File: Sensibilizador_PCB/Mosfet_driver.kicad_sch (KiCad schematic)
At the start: 11 parts, among them U1 LM5104M

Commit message: Rectificador primera versión
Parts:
- renumbered C2 to C?, C1 to C?, C3 to C?, D2 to D?, D1 to D?, R4 to R?, R2 to R?, R3 to R?, R1 to R?, U1 to U?
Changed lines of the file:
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@@
     (effects (font (size 1.27 1.27)) (justify left))
   )
-  (symbol (lib_id "Device:C_Polarized") (at 58.42 67.31 0) (unit 1)
+  (symbol (lib_id "Device:C_Polarized") (at 58.42 67.31 0)
     (in_bom yes) (on_board yes)
-    (property "Reference" "C2" (id 0) (at 64.77 68.58 90)
+    (property "Reference" "C?" (id 0) (at 64.77 68.58 90)
       (effects (font (size 1.27 1.27)) (justify left))
     )
@@
     (pin "2")
   )
-  (symbol (lib_id "Device:R") (at 105.41 80.01 0) (unit 1)
+  (symbol (lib_id "Device:R") (at 105.41 80.01 0)
     (in_bom yes) (on_board yes) (fields_autoplaced)
-    (property "Reference" "R4" (id 0) (at 107.95 78.7399 0)
+    (property "Reference" "R?" (id 0) (at 107.95 78.7399 0)
       (effects (font (size 1.27 1.27)) (justify left))
     )
@@
     (pin "2")
   )
-  (symbol (lib_id "Device:C_Polarized") (at 48.26 67.31 0) (unit 1)
+  (symbol (lib_id "Device:C_Polarized") (at 48.26 67.31 0)
     (in_bom yes) (on_board yes)
-    (property "Reference" "C1" (id 0) (at 52.07 68.58 90)
+    (property "Reference" "C?" (id 0) (at 52.07 68.58 90)
       (effects (font (size 1.27 1.27)) (justify left))
     )
@@
     (pin "2")
   )
-  (symbol (lib_id "Device:R") (at 109.22 63.5 90) (unit 1)
+  (symbol (lib_id "Device:R") (at 109.22 63.5 90)
     (in_bom yes) (on_board yes)
-    (property "Reference" "R2" (id 0) (at 109.22 60.96 90))
+    (property "Reference" "R?" (id 0) (at 109.22 60.96 90))
     (property "Value" " 2.74 1{slash}4W" (id 1) (at 109.22 66.04 90))
     (property "Footprint" "Resistor_SMD:R_1206_3216Metric_Pad1.30x1.75mm_HandSolder" (id 2) (at 109.22 65.278 90)
@@
     (pin "2")
   )
-  (symbol (lib_id "Device:D") (at 118.11 63.5 0) (unit 1)
+  (symbol (lib_id "Device:D") (at 118.11 63.5 0)
     (in_bom yes) (on_board yes)
-    (property "Reference" "D2" (id 0) (at 119.38 60.96 0))
+    (property "Reference" "D?" (id 0) (at 119.38 60.96 0))
     (property "Value" "SS34FA" (id 1) (at 119.38 66.04 0))
     (property "Footprint" "Diode_SMD:D_SOD-123" (id 2) (at 118.11 63.5 0)
@@
     (pin "2")
   )
-  (symbol (lib_id "Device:R") (at 115.57 68.58 90) (unit 1)
+  (symbol (lib_id "Device:R") (at 115.57 68.58 90)
     (in_bom yes) (on_board yes)
-    (property "Reference" "R3" (id 0) (at 115.57 71.12 90))
+    (property "Reference" "R?" (id 0) (at 115.57 71.12 90))
     (property "Value" " 2.74 1{slash}4W" (id 1) (at 115.57 73.66 90))
     (property "Footprint" "Resistor_SMD:R_1206_3216Metric_Pad1.30x1.75mm_HandSolder" (id 2) (at 115.57 70.358 90)
@@
     (pin "2")
   )
-  (symbol (lib_id "Device:C_Polarized") (at 88.9 39.37 90) (unit 1)
+  (symbol (lib_id "Device:C_Polarized") (at 88.9 39.37 90)
     (in_bom yes) (on_board yes)
-    (property "Reference" "C3" (id 0) (at 90.17 33.02 90)
+    (property "Reference" "C?" (id 0) (at 90.17 33.02 90)
       (effects (font (size 1.27 1.27)) (justify left))
     )
@@
     (pin "2")
   )
-  (symbol (lib_id "Device:R") (at 109.22 45.72 90) (unit 1)
+  (symbol (lib_id "Device:R") (at 109.22 45.72 90)
     (in_bom yes) (on_board yes)
-    (property "Reference" "R1" (id 0) (at 109.22 48.26 90))
+    (property "Reference" "R?" (id 0) (at 109.22 48.26 90))
     (property "Value" " 2.74 1{slash}4W" (id 1) (at 109.22 43.18 90))
     (property "Footprint" "Resistor_SMD:R_1206_3216Metric_Pad1.30x1.75mm_HandSolder" (id 2) (at 109.22 47.498 90)
@@
     (pin "2")
   )
-  (symbol (lib_id "Device:D") (at 118.11 45.72 0) (unit 1)
+  (symbol (lib_id "Device:D") (at 118.11 45.72 0)
     (in_bom yes) (on_board yes)
-    (property "Reference" "D1" (id 0) (at 120.65 40.64 0))
+    (property "Reference" "D?" (id 0) (at 120.65 40.64 0))
     (property "Value" "SS34FA" (id 1) (at 120.65 43.18 0))
     (property "Footprint" "Diode_SMD:D_SOD-123" (id 2) (at 118.11 45.72 0)
@@
     (pin "2")
   )
-  (symbol (lib_id "Device:R") (at 118.11 52.07 90) (unit 1)
+  (symbol (lib_id "Device:R") (at 118.11 52.07 90)
     (in_bom yes) (on_board yes)
     (property "Reference" "RHon?" (id 0) (at 118.11 54.61 90))
@@
     (pin "2")
   )
-  (symbol (lib_id "LM5104M:LM5104M") (at 82.55 63.5 0) (unit 1)
+  (symbol (lib_id "LM5104M:LM5104M") (at 82.55 63.5 0)
     (in_bom yes) (on_board yes) (fields_autoplaced)
-    (property "Reference" "U1" (id 0) (at 84.4297 43.18 0)
+    (property "Reference" "U?" (id 0) (at 84.4297 43.18 0)
       (effects (font (size 1.27 1.27)) (justify left))
     )

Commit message: Listo pa tirar lineas
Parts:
- R1: renamed from R?; footprint Resistor_SMD:R_1206_3216Metric_Pad1.30x1.75mm_HandSolder -> Resistor_SMD:R_0805_2012Metric_Pad1.20x1.40mm_HandSolder
- U1: renamed from U?; footprint Package_SO:SOIC-8-1EP_3.9x4.9mm_P1.27mm_EP2.29x3mm -> Package_SO:SOIC-8_3.9x4.9mm_P1.27mm
- gave numbers to parts that had none: 9
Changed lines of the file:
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@@
     (effects (font (size 1.27 1.27)) (justify left))
   )
-  (symbol (lib_id "Device:C_Polarized") (at 58.42 67.31 0)
+  (symbol (lib_id "Device:C_Polarized") (at 58.42 67.31 0) (unit 1)
     (in_bom yes) (on_board yes)
-    (property "Reference" "C?" (id 0) (at 64.77 68.58 90)
+    (property "Reference" "C2" (id 0) (at 64.77 68.58 90)
       (effects (font (size 1.27 1.27)) (justify left))
     )
@@
     (pin "2")
   )
-  (symbol (lib_id "Device:R") (at 105.41 80.01 0)
+  (symbol (lib_id "Device:R") (at 105.41 80.01 0) (unit 1)
     (in_bom yes) (on_board yes) (fields_autoplaced)
-    (property "Reference" "R?" (id 0) (at 107.95 78.7399 0)
+    (property "Reference" "R1" (id 0) (at 107.95 78.7399 0)
       (effects (font (size 1.27 1.27)) (justify left))
     )
@@
       (effects (font (size 1.27 1.27)) (justify left))
     )
-    (property "Footprint" "Resistor_SMD:R_1206_3216Metric_Pad1.30x1.75mm_HandSolder" (id 2) (at 103.632 80.01 90)
+    (property "Footprint" "Resistor_SMD:R_0805_2012Metric_Pad1.20x1.40mm_HandSolder" (id 2) (at 103.632 80.01 90)
       (effects (font (size 1.27 1.27)) hide)
     )
@@
     (pin "2")
   )
-  (symbol (lib_id "Device:C_Polarized") (at 48.26 67.31 0)
+  (symbol (lib_id "Device:C_Polarized") (at 48.26 67.31 0) (unit 1)
     (in_bom yes) (on_board yes)
-    (property "Reference" "C?" (id 0) (at 52.07 68.58 90)
+    (property "Reference" "C1" (id 0) (at 52.07 68.58 90)
       (effects (font (size 1.27 1.27)) (justify left))
     )
@@
     (pin "2")
   )
-  (symbol (lib_id "Device:R") (at 109.22 63.5 90)
+  (symbol (lib_id "Device:R") (at 109.22 63.5 90) (unit 1)
     (in_bom yes) (on_board yes)
-    (property "Reference" "R?" (id 0) (at 109.22 60.96 90))
+    (property "Reference" "R3" (id 0) (at 109.22 60.96 90))
     (property "Value" " 2.74 1{slash}4W" (id 1) (at 109.22 66.04 90))
     (property "Footprint" "Resistor_SMD:R_1206_3216Metric_Pad1.30x1.75mm_HandSolder" (id 2) (at 109.22 65.278 90)
@@
     (pin "2")
   )
-  (symbol (lib_id "Device:D") (at 118.11 63.5 0)
+  (symbol (lib_id "Device:D") (at 118.11 63.5 0) (unit 1)
     (in_bom yes) (on_board yes)
-    (property "Reference" "D?" (id 0) (at 119.38 60.96 0))
+    (property "Reference" "D6" (id 0) (at 119.38 60.96 0))
     (property "Value" "SS34FA" (id 1) (at 119.38 66.04 0))
     (property "Footprint" "Diode_SMD:D_SOD-123" (id 2) (at 118.11 63.5 0)
@@
     (pin "2")
   )
-  (symbol (lib_id "Device:R") (at 115.57 68.58 90)
+  (symbol (lib_id "Device:R") (at 115.57 68.58 90) (unit 1)
     (in_bom yes) (on_board yes)
-    (property "Reference" "R?" (id 0) (at 115.57 71.12 90))
+    (property "Reference" "R4" (id 0) (at 115.57 71.12 90))
     (property "Value" " 2.74 1{slash}4W" (id 1) (at 115.57 73.66 90))
     (property "Footprint" "Resistor_SMD:R_1206_3216Metric_Pad1.30x1.75mm_HandSolder" (id 2) (at 115.57 70.358 90)
@@
     (pin "2")
   )
-  (symbol (lib_id "Device:C_Polarized") (at 88.9 39.37 90)
+  (symbol (lib_id "Device:C_Polarized") (at 88.9 39.37 90) (unit 1)
     (in_bom yes) (on_board yes)
-    (property "Reference" "C?" (id 0) (at 90.17 33.02 90)
+    (property "Reference" "C3" (id 0) (at 90.17 33.02 90)
       (effects (font (size 1.27 1.27)) (justify left))
     )
@@
     (pin "2")
   )
-  (symbol (lib_id "Device:R") (at 109.22 45.72 90)
+  (symbol (lib_id "Device:R") (at 109.22 45.72 90) (unit 1)
     (in_bom yes) (on_board yes)
-    (property "Reference" "R?" (id 0) (at 109.22 48.26 90))
+    (property "Reference" "R2" (id 0) (at 109.22 48.26 90))
     (property "Value" " 2.74 1{slash}4W" (id 1) (at 109.22 43.18 90))
     (property "Footprint" "Resistor_SMD:R_1206_3216Metric_Pad1.30x1.75mm_HandSolder" (id 2) (at 109.22 47.498 90)
@@
     (pin "2")
   )
-  (symbol (lib_id "Device:D") (at 118.11 45.72 0)
+  (symbol (lib_id "Device:D") (at 118.11 45.72 0) (unit 1)
     (in_bom yes) (on_board yes)
-    (property "Reference" "D?" (id 0) (at 120.65 40.64 0))
+    (property "Reference" "D5" (id 0) (at 120.65 40.64 0))
     (property "Value" "SS34FA" (id 1) (at 120.65 43.18 0))
     (property "Footprint" "Diode_SMD:D_SOD-123" (id 2) (at 118.11 45.72 0)
@@
     (pin "2")
   )
-  (symbol (lib_id "Device:R") (at 118.11 52.07 90)
+  (symbol (lib_id "Device:R") (at 118.11 52.07 90) (unit 1)
     (in_bom yes) (on_board yes)
-    (property "Reference" "RHon?" (id 0) (at 118.11 54.61 90))
+    (property "Reference" "RHon1" (id 0) (at 118.11 54.61 90))
     (property "Value" " 2.74 1{slash}4W" (id 1) (at 118.11 49.53 90))
     (property "Footprint" "Resistor_SMD:R_1206_3216Metric_Pad1.30x1.75mm_HandSolder" (id 2) (at 118.11 53.848 90)
@@
     (pin "2")
   )
-  (symbol (lib_id "LM5104M:LM5104M") (at 82.55 63.5 0)
+  (symbol (lib_id "LM5104M:LM5104M") (at 82.55 63.5 0) (unit 1)
     (in_bom yes) (on_board yes) (fields_autoplaced)
-    (property "Reference" "U?" (id 0) (at 84.4297 43.18 0)
+    (property "Reference" "U1" (id 0) (at 84.4297 43.18 0)
       (effects (font (size 1.27 1.27)) (justify left))
     )
@@
       (effects (font (size 1.27 1.27)) (justify left))
     )
-    (property "Footprint" "Package_SO:SOIC-8-1EP_3.9x4.9mm_P1.27mm_EP2.29x3mm" (id 2) (at 82.55 63.5 0)
+    (property "Footprint" "Package_SO:SOIC-8_3.9x4.9mm_P1.27mm" (id 2) (at 82.55 63.5 0)
       (effects (font (size 1.27 1.27)) (justify left bottom) hide)
     )

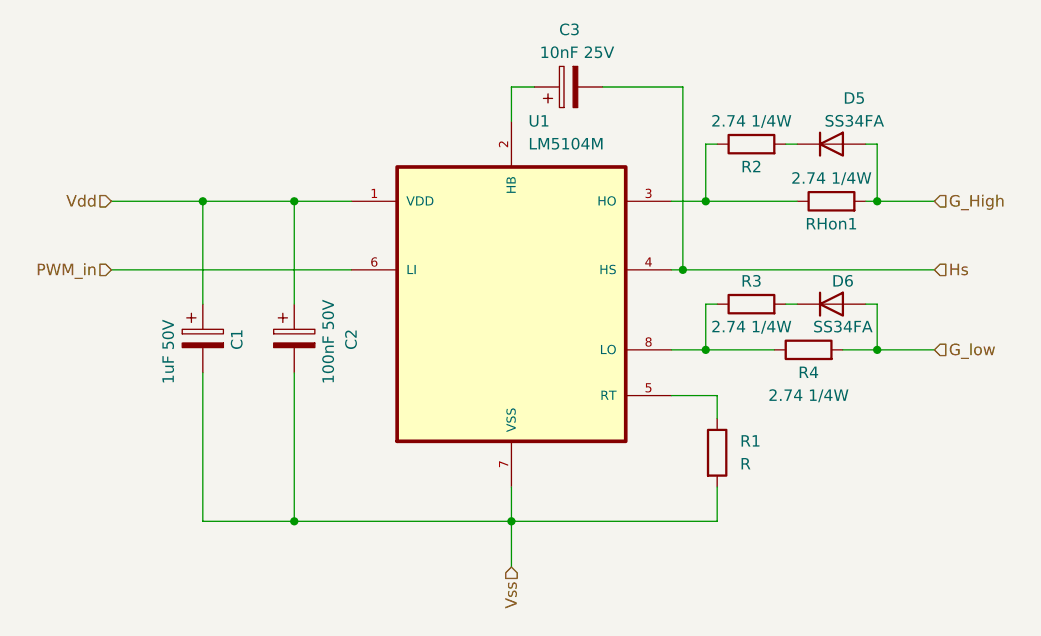
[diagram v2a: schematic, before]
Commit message: mini cambio en label de RHon
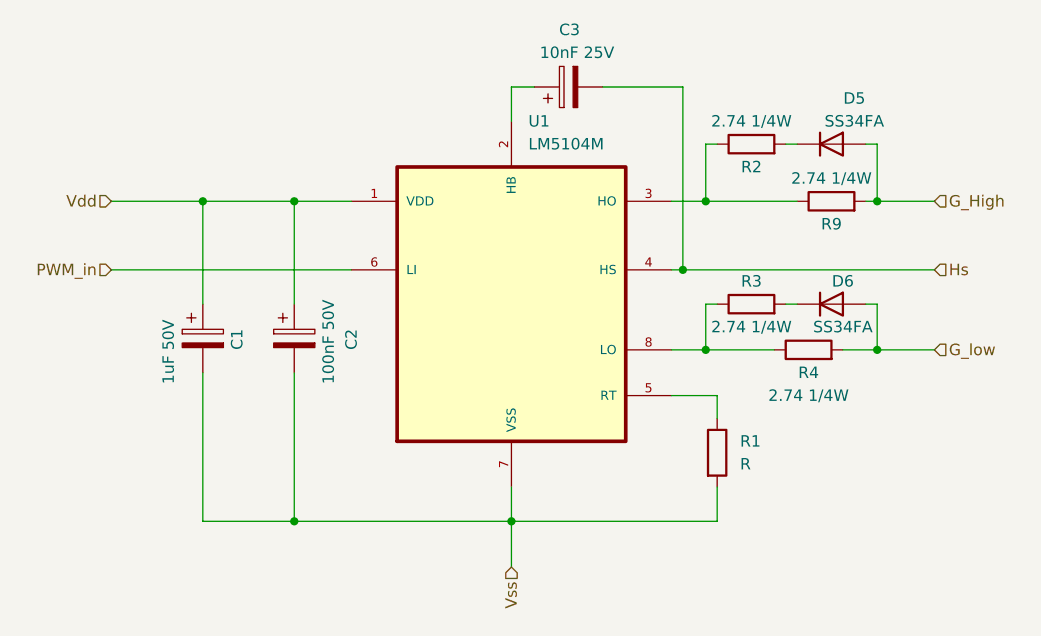
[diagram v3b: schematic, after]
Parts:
- renumbered RHon1 to R9
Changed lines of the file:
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@@
   (symbol (lib_id "Device:R") (at 118.11 52.07 90) (unit 1)
     (in_bom yes) (on_board yes)
-    (property "Reference" "RHon1" (id 0) (at 118.11 54.61 90))
+    (property "Reference" "R9" (id 0) (at 118.11 54.61 90))
     (property "Value" " 2.74 1{slash}4W" (id 1) (at 118.11 49.53 90))
     (property "Footprint" "Resistor_SMD:R_1206_3216Metric_Pad1.30x1.75mm_HandSolder" (id 2) (at 118.11 53.848 90)

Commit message: ValoresCorregidos
Algunos valores de resistencias fueron corregidos y coinciden con la placa.
Valores de resistencias en los leds.
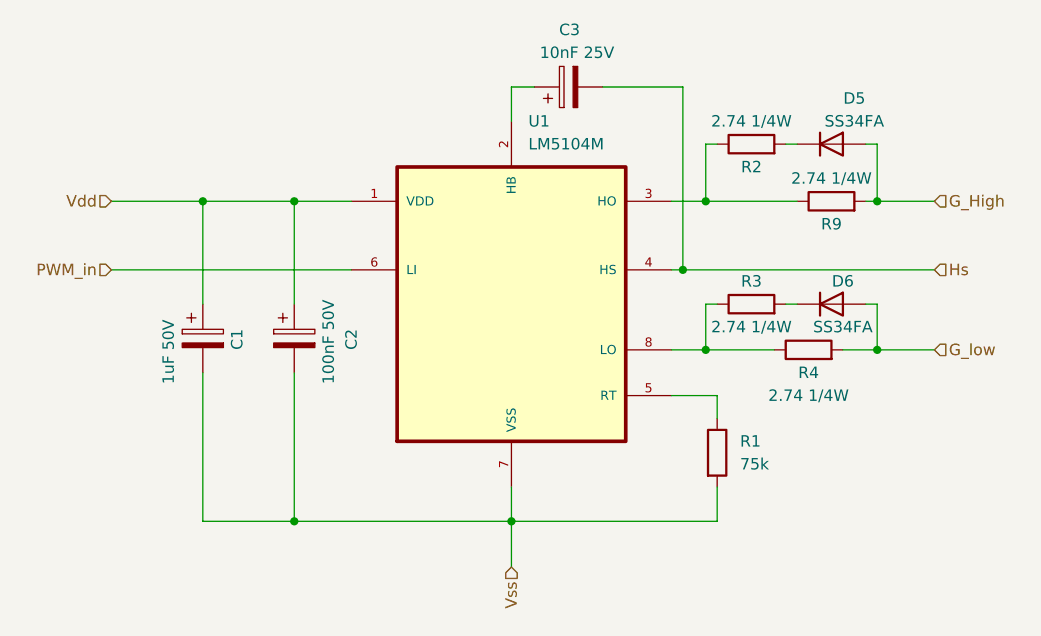
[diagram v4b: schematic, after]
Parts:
- R1: value R -> 75k
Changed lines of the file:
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@@
     (effects (font (size 1.27 1.27)) (justify left))
   )
-  (symbol (lib_id "Device:C_Polarized") (at 58.42 67.31 0) (unit 1)
+  (symbol (lib_id "Device:C_Polarized") (at 58.42 67.31 0)
     (in_bom yes) (on_board yes)
     (property "Reference" "C2" (id 0) (at 64.77 68.58 90)
@@
     (pin "2")
   )
-  (symbol (lib_id "Device:R") (at 105.41 80.01 0) (unit 1)
+  (symbol (lib_id "Device:R") (at 105.41 80.01 0)
     (in_bom yes) (on_board yes) (fields_autoplaced)
     (property "Reference" "R1" (id 0) (at 107.95 78.7399 0)
       (effects (font (size 1.27 1.27)) (justify left))
     )
-    (property "Value" "R" (id 1) (at 107.95 81.2799 0)
+    (property "Value" "75k" (id 1) (at 107.95 81.2799 0)
       (effects (font (size 1.27 1.27)) (justify left))
     )
@@
     (pin "2")
   )
-  (symbol (lib_id "Device:C_Polarized") (at 48.26 67.31 0) (unit 1)
+  (symbol (lib_id "Device:C_Polarized") (at 48.26 67.31 0)
     (in_bom yes) (on_board yes)
     (property "Reference" "C1" (id 0) (at 52.07 68.58 90)
@@
     (pin "2")
   )
-  (symbol (lib_id "Device:R") (at 109.22 63.5 90) (unit 1)
+  (symbol (lib_id "Device:R") (at 109.22 63.5 90)
     (in_bom yes) (on_board yes)
     (property "Reference" "R3" (id 0) (at 109.22 60.96 90))
@@
     (pin "2")
   )
-  (symbol (lib_id "Device:D") (at 118.11 63.5 0) (unit 1)
+  (symbol (lib_id "Device:D") (at 118.11 63.5 0)
     (in_bom yes) (on_board yes)
     (property "Reference" "D6" (id 0) (at 119.38 60.96 0))
@@
     (pin "2")
   )
-  (symbol (lib_id "Device:R") (at 115.57 68.58 90) (unit 1)
+  (symbol (lib_id "Device:R") (at 115.57 68.58 90)
     (in_bom yes) (on_board yes)
     (property "Reference" "R4" (id 0) (at 115.57 71.12 90))
@@
     (pin "2")
   )
-  (symbol (lib_id "Device:C_Polarized") (at 88.9 39.37 90) (unit 1)
+  (symbol (lib_id "Device:C_Polarized") (at 88.9 39.37 90)
     (in_bom yes) (on_board yes)
     (property "Reference" "C3" (id 0) (at 90.17 33.02 90)
@@
     (pin "2")
   )
-  (symbol (lib_id "Device:R") (at 109.22 45.72 90) (unit 1)
+  (symbol (lib_id "Device:R") (at 109.22 45.72 90)
     (in_bom yes) (on_board yes)
     (property "Reference" "R2" (id 0) (at 109.22 48.26 90))
@@
     (pin "2")
   )
-  (symbol (lib_id "Device:D") (at 118.11 45.72 0) (unit 1)
+  (symbol (lib_id "Device:D") (at 118.11 45.72 0)
     (in_bom yes) (on_board yes)
     (property "Reference" "D5" (id 0) (at 120.65 40.64 0))
@@
     (pin "2")
   )
-  (symbol (lib_id "Device:R") (at 118.11 52.07 90) (unit 1)
+  (symbol (lib_id "Device:R") (at 118.11 52.07 90)
     (in_bom yes) (on_board yes)
     (property "Reference" "R9" (id 0) (at 118.11 54.61 90))
@@
     (pin "2")
   )
-  (symbol (lib_id "LM5104M:LM5104M") (at 82.55 63.5 0) (unit 1)
+  (symbol (lib_id "LM5104M:LM5104M") (at 82.55 63.5 0)
     (in_bom yes) (on_board yes) (fields_autoplaced)
     (property "Reference" "U1" (id 0) (at 84.4297 43.18 0)
